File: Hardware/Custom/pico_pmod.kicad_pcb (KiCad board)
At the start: 2 copper layers, 50 x 37 mm, 22 parts, among them J1 Conn_02x06_Odd_Even, J2 Conn_02x06_Odd_Even, J3 Conn_02x06_Odd_Even, J4 USB_C_Receptacle_USB2.0, U1 RP2040

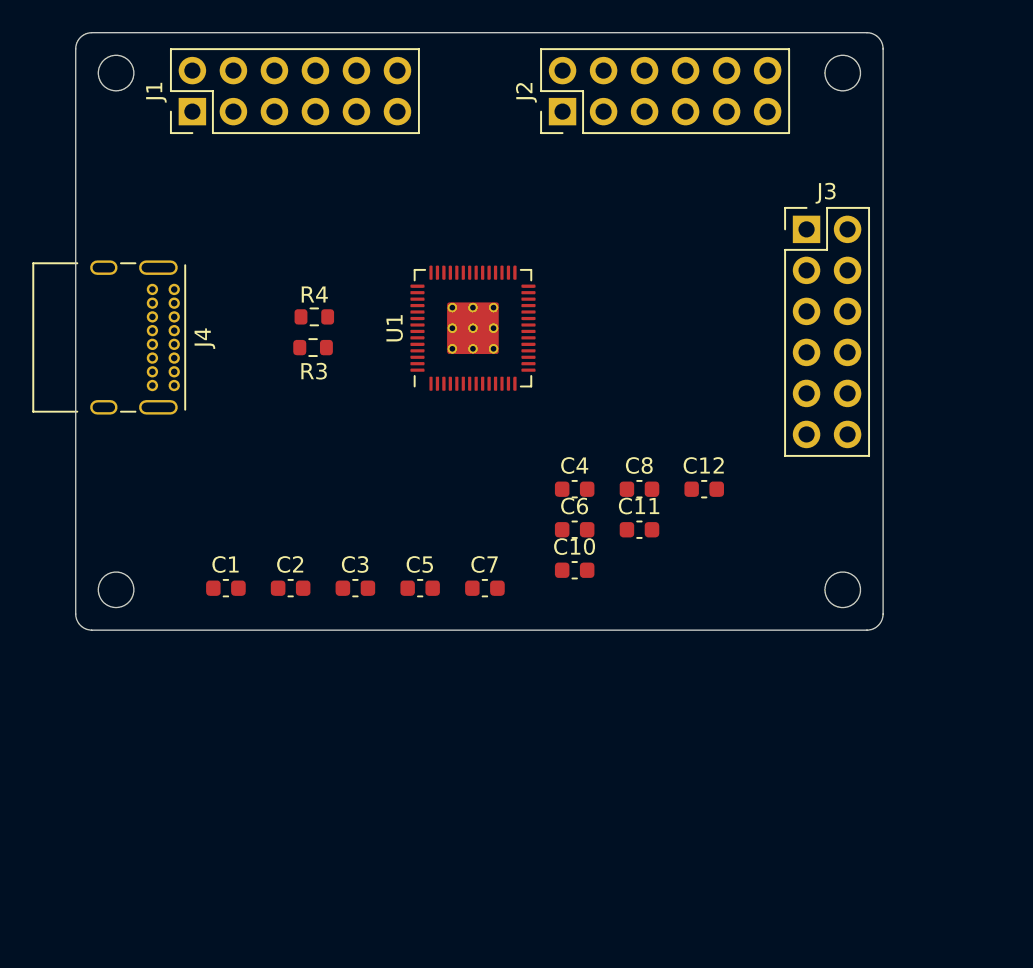
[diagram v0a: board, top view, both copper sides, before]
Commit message: Add the switchs footprints and put on PCB
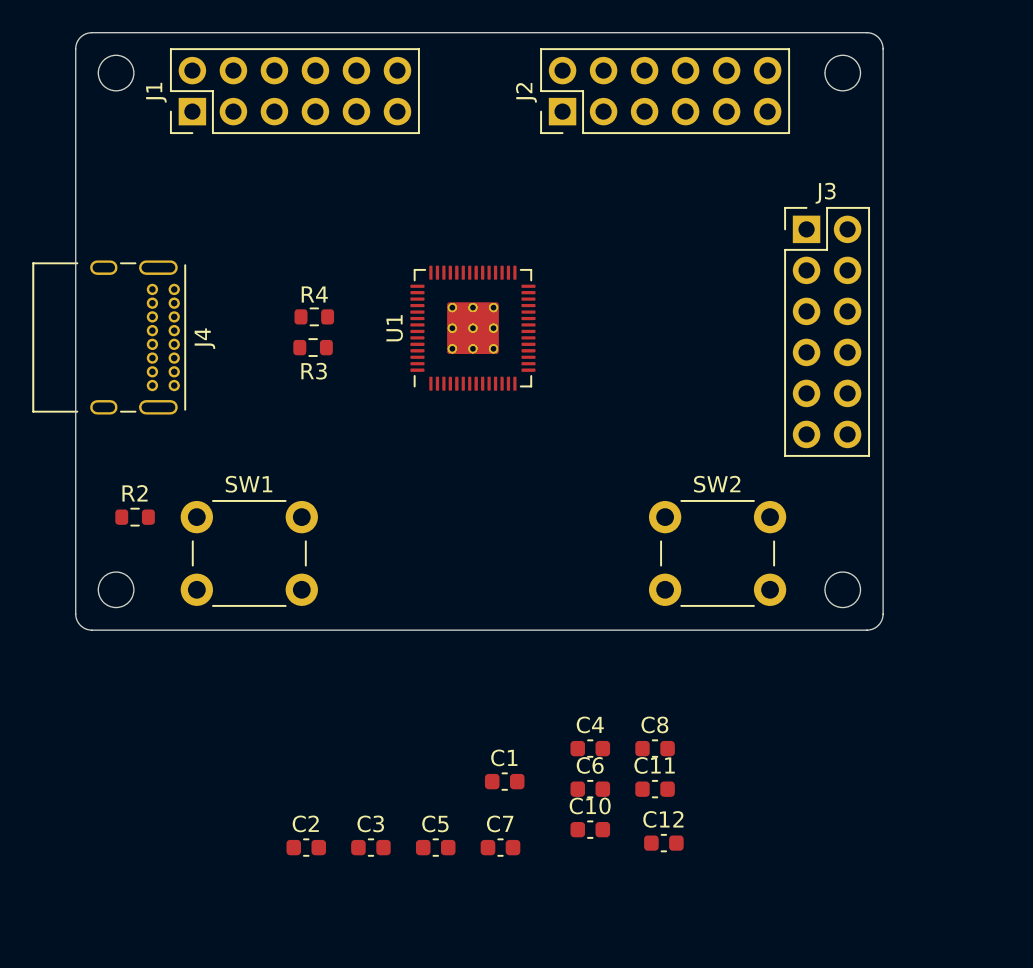
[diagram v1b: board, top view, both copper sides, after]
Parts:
- added R2: 1K, Resistor_SMD:R_0603_1608Metric, F.Cu at (126.7, 87.0)
- added SW1: SW_Push, Button_Switch_THT:SW_PUSH_6mm_H4.3mm, F.Cu at (130.5, 87.0)
- added SW2: SW_Push, Button_Switch_THT:SW_PUSH_6mm_H4.3mm, F.Cu at (159.5, 87.0)
- moved C12 22.1 mm to (159.4, 107.2)
- moved C1 21.0 mm to (149.6, 103.4)
- moved C10 16.1 mm to (154.9, 106.4)
- moved C11 16.1 mm to (158.9, 103.8)
- moved C2 16.1 mm to (137.3, 107.5)
- moved C3 16.1 mm to (141.3, 107.5)
- moved C4 16.1 mm to (154.9, 101.3)
- moved C5 16.1 mm to (145.3, 107.5)
- moved C6 16.1 mm to (154.9, 103.8)
- moved C7 16.1 mm to (149.3, 107.5)
- moved C8 16.1 mm to (158.9, 101.3)
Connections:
- J1 pad 1: GPIO_1 -> Net-(J1-Pad1)
- J1 pad 2: GPIO_0 -> Net-(J1-Pad2)
- J1 pad 3: GPIO_3 -> Net-(J1-Pad3)
- J1 pad 4: GPIO_2 -> Net-(J1-Pad4)
- J1 pad 5: GPIO_5 -> Net-(J1-Pad5)
- J1 pad 6: GPIO_4 -> Net-(J1-Pad6)
- J1 pad 7: GPIO_7 -> Net-(J1-Pad7)
- J1 pad 8: GPIO_6 -> Net-(J1-Pad8)
- J3 pad 1: Net-(J3-Pad1) -> GPIO_7
- J3 pad 2: Net-(J3-Pad2) -> GPIO_6
- J3 pad 3: Net-(J3-Pad3) -> GPIO_5
- J3 pad 4: Net-(J3-Pad4) -> GPIO_4
- J3 pad 5: Net-(J3-Pad5) -> GPIO_3
- J3 pad 6: Net-(J3-Pad6) -> GPIO_2
- J3 pad 7: Net-(J3-Pad7) -> GPIO_1
- J3 pad 8: Net-(J3-Pad8) -> GPIO_0

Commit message: Add usb CC 1 and 2 resistors
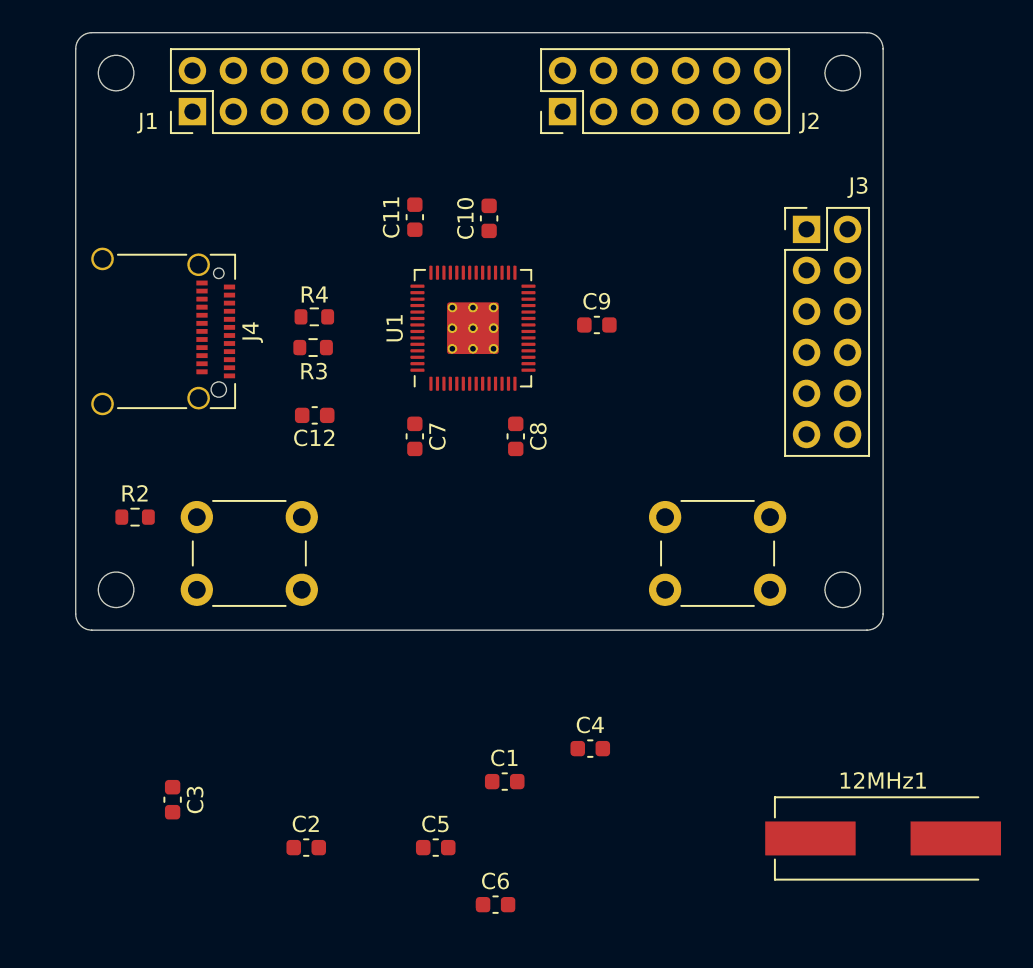
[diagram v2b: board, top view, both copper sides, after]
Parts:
- added 12MHz1: Crystal, RaspberryPi:Crystal_SMD_HC49-US, F.Cu at (173.0, 106.9)
- added C9: 100n, Capacitor_SMD:C_0603_1608Metric, F.Cu at (155.3, 75.1)
- C2, C4: value C -> 27p
- J4: footprint Connector_USB:USB_C_Receptacle_GCT_USB4085 -> Connector_USB:USB_C_Receptacle_Amphenol_12401610E4-2A_CircularHoles
- moved C11 38.4 mm to (144.0, 68.4), turned to 90 degrees
- moved C10 38.4 mm to (148.6, 68.5), turned to 90 degrees
- moved C12 34.2 mm to (137.8, 80.7), turned to 180 degrees
- moved C7 26.0 mm to (144.0, 82.0), turned to 270 degrees
- moved C8 21.2 mm to (150.2, 82.0), turned to 270 degrees
- moved C3 12.6 mm to (129.0, 104.5), turned to 270 degrees
- moved C6 9.25 mm to (149.0, 111.0)
- moved J4 3.05 mm to (127.5, 75.5)

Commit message: Add power supply and spi memory
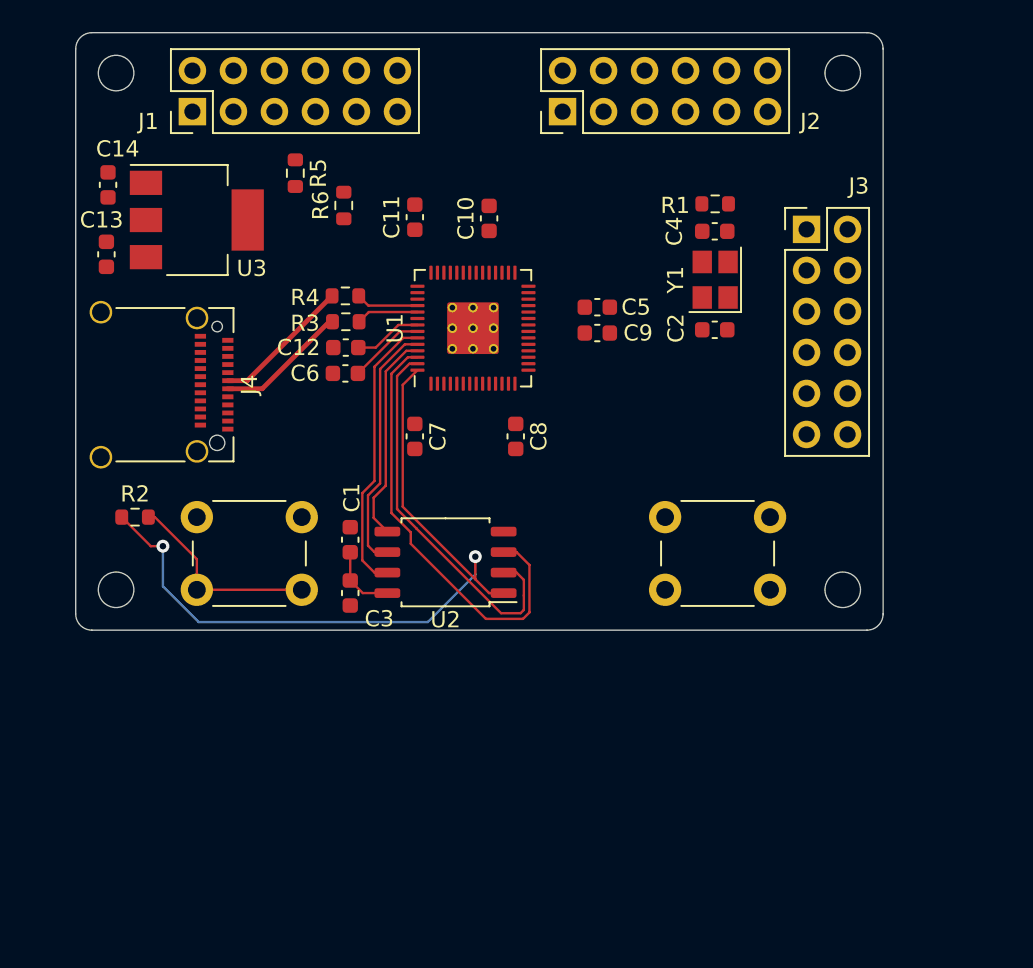
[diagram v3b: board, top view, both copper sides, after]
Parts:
- removed 12MHz1: Crystal, RaspberryPi:Crystal_SMD_HC49-US
- added C13: 10u, Capacitor_SMD:C_0603_1608Metric, F.Cu at (124.9, 70.7)
- added C14: 10u, Capacitor_SMD:C_0603_1608Metric, F.Cu at (125.0, 66.4)
- added R1: 1K, Resistor_SMD:R_0603_1608Metric, F.Cu at (162.6, 67.6)
- added R5: 5.1k, Resistor_SMD:R_0603_1608Metric, F.Cu at (136.6, 65.7)
- added R6: 5.1k, Resistor_SMD:R_0603_1608Metric, F.Cu at (139.6, 67.7)
- added U2: W25Q128JVS, Package_SO:SOIC-8_5.23x5.23mm_P1.27mm, F.Cu at (145.9, 89.8)
- added U3: NCP1117-3.3_SOT223, Package_TO_SOT_SMD:SOT-223-3_TabPin2, F.Cu at (130.5, 68.6)
- added Y1: 12MHz, Crystal:Crystal_SMD_SeikoEpson_FA238-4Pin_3.2x2.5mm, F.Cu at (162.6, 72.3)
- C2, C4: value 27p -> 20p
- moved C2 40.8 mm to (162.6, 75.4), turned to 180 degrees
- moved C5 34.9 mm to (155.3, 74.0)
- moved C6 34.2 mm to (139.7, 78.1), turned to 180 degrees
- moved C4 33.0 mm to (162.6, 69.3)
- moved C1 17.8 mm to (140.0, 88.4), turned to 90 degrees
- moved C3 16.9 mm to (140.0, 91.7)
- moved C12 4.62 mm to (139.7, 76.5)
- moved J4 3.30 mm to (127.4, 78.8)
- moved R3 2.58 mm to (139.7, 74.9)
- moved R4 2.32 mm to (139.7, 73.3)
- moved C9 0.50 mm to (155.3, 75.6)
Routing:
- net QSPI_SS: track 0.00 -> 47.9 mm, vias 0 -> 2
- net QSPI_SD2: track 0.00 -> 27.4 mm
- net QSPI_SD1: track 0.00 -> 23.7 mm
- net QSPI_SD3: track 0.00 -> 17.6 mm
- net QSPI_SCLK: track 0.00 -> 15.6 mm
- net QSPI_SD0: track 0.00 -> 13.1 mm
- net Net-(R2-Pad2): track 0.00 -> 12.5 mm
- net USB_DP: track 0.00 -> 8.63 mm
- net +3V3: track 0.00 -> 8.62 mm
- net USB_DN: track 0.00 -> 8.20 mm
- net +1V1: track 0.00 -> 4.76 mm
- net Net-(R4-Pad2): track 0.00 -> 3.89 mm
- net Net-(R3-Pad2): track 0.00 -> 3.86 mm
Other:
- rule trace_min: 0.2 -> 0.127

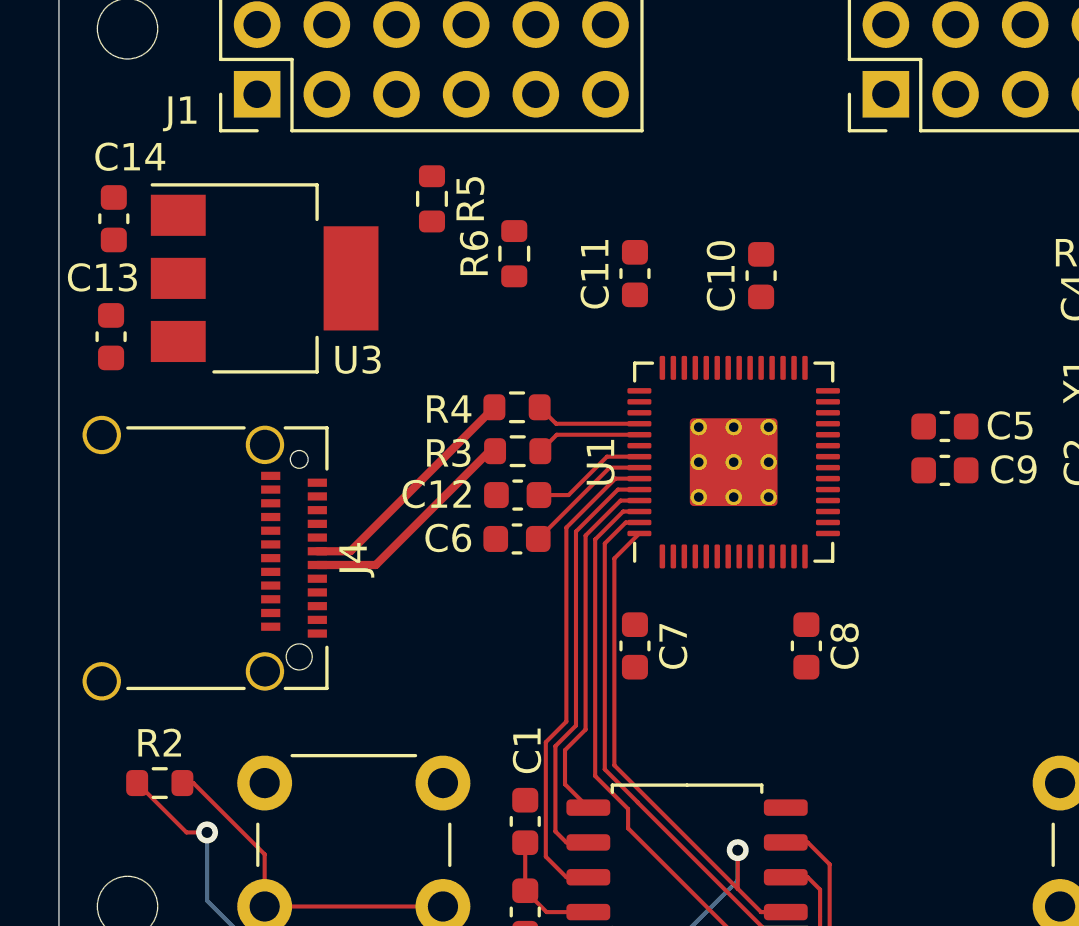
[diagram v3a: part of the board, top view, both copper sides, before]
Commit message: Add the USB resitors and route power supply
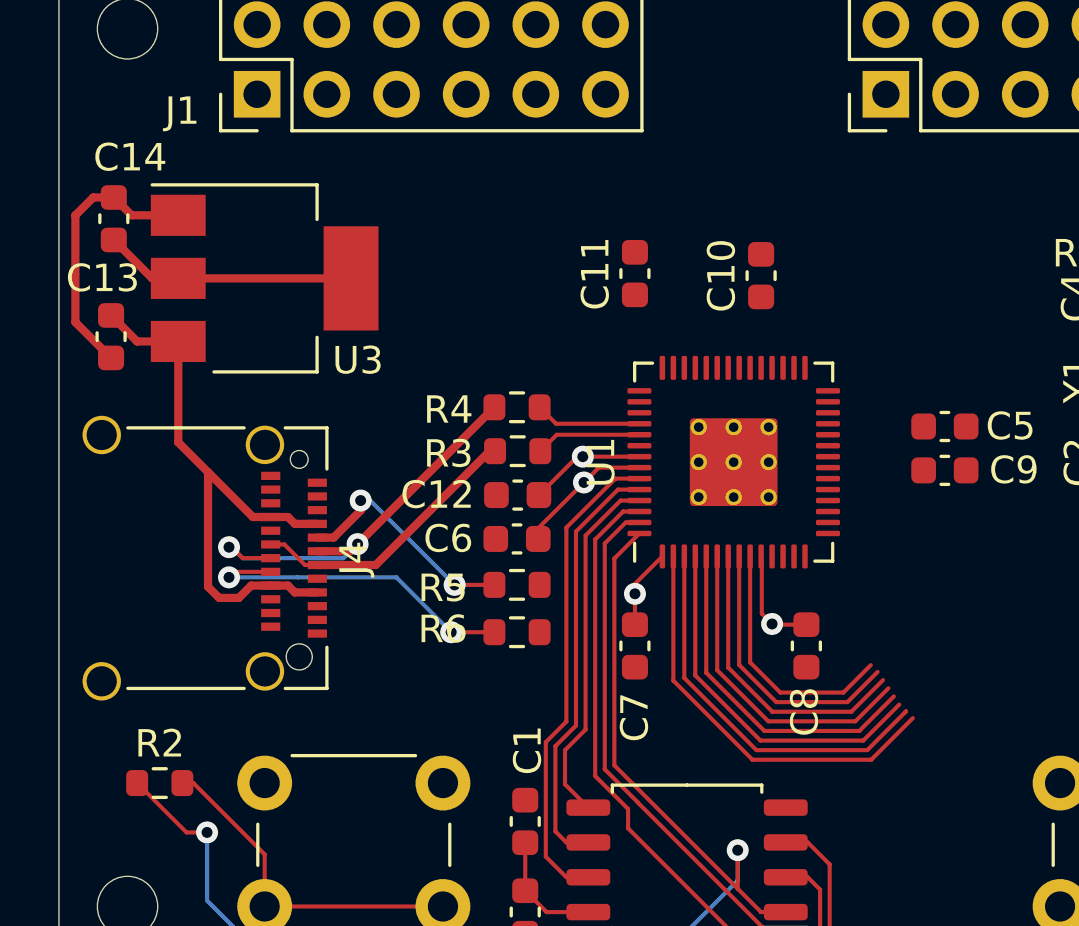
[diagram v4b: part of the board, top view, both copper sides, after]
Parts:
- moved R5 14.4 mm to (139.7, 79.8), turned to 180 degrees
- moved R6 13.8 mm to (139.7, 81.5), turned to 0 degrees
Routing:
- net VBUS: track 0.00 -> 21.4 mm
- net +3V3: track 8.62 -> 24.6 mm, vias 0 -> 3
- net GPIO_0: track 0.00 -> 15.1 mm
- net GPIO_1: track 0.00 -> 14.3 mm
- net GPIO_2: track 0.00 -> 13.3 mm
- net GPIO_3: track 0.00 -> 12.5 mm
- net Net-(J4-PadB5): track 0.00 -> 12.1 mm, vias 0 -> 2
- net GPIO_4: track 0.00 -> 11.7 mm
- net GPIO_5: track 0.00 -> 10.8 mm
- net GND: track 0.00 -> 10.0 mm
- net GPIO_6: track 0.00 -> 10.0 mm
- net GPIO_7: track 0.00 -> 9.13 mm
- net Net-(J4-PadA5): track 0.00 -> 8.60 mm, vias 0 -> 2
- net USB_DP: track 8.63 -> 15.4 mm, vias 0 -> 2
- net USB_DN: track 8.20 -> 10.2 mm
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
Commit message: Add the debug port footprint
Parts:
- added J5: Conn_01x04, Connector_PinHeader_2.54mm:PinHeader_1x04_P2.54mm_Vertical, F.Cu at (156.1, 103.9)
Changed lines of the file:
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@@
     (tracks 195)
     (zones 0)
-    (modules 34)
+    (modules 35)
     (nets 76)
   )
@@
     (add_net XOUT)
   )
+  (module Connector_PinHeader_2.54mm:PinHeader_1x04_P2.54mm_Vertical (layer F.Cu)
+    (at 156.1 103.9)
+    (descr "Through hole straight pin header, 1x04, 2.54mm pitch, single row")
+    (tags "Through hole pin header THT 1x04 2.54mm single row")
+    (fp_text reference J5 (at 0 -2.33) (layer F.SilkS)
+      (effects (font (size 1 1) (thickness 0.15)))
+    )
+    (fp_text value Conn_01x04 (at 0 9.95) (layer F.Fab)
+      (effects (font (size 1 1) (thickness 0.15)))
+    )
+    (fp_text user %R (at 0 3.81 90) (layer F.Fab)
+      (effects (font (size 1 1) (thickness 0.15)))
+    )
+    (fp_line (start -0.635 -1.27) (end 1.27 -1.27) (layer F.Fab) (width 0.1))
+    (fp_line (start 1.27 -1.27) (end 1.27 8.89) (layer F.Fab) (width 0.1))
+    (fp_line (start 1.27 8.89) (end -1.27 8.89) (layer F.Fab) (width 0.1))
+    (fp_line (start -1.27 8.89) (end -1.27 -0.635) (layer F.Fab) (width 0.1))
+    (fp_line (start -1.27 -0.635) (end -0.635 -1.27) (layer F.Fab) (width 0.1))
+    (fp_line (start -1.33 8.95) (end 1.33 8.95) (layer F.SilkS) (width 0.12))
+    (fp_line (start -1.33 1.27) (end -1.33 8.95) (layer F.SilkS) (width 0.12))
+    (fp_line (start 1.33 1.27) (end 1.33 8.95) (layer F.SilkS) (width 0.12))
+    (fp_line (start -1.33 1.27) (end 1.33 1.27) (layer F.SilkS) (width 0.12))
+    (fp_line (start -1.33 0) (end -1.33 -1.33) (layer F.SilkS) (width 0.12))
+    (fp_line (start -1.33 -1.33) (end 0 -1.33) (layer F.SilkS) (width 0.12))
+    (fp_line (start -1.8 -1.8) (end -1.8 9.4) (layer F.CrtYd) (width 0.05))
+    (fp_line (start -1.8 9.4) (end 1.8 9.4) (layer F.CrtYd) (width 0.05))
+    (fp_line (start 1.8 9.4) (end 1.8 -1.8) (layer F.CrtYd) (width 0.05))
+    (fp_line (start 1.8 -1.8) (end -1.8 -1.8) (layer F.CrtYd) (width 0.05))
+    (pad 4 thru_hole oval (at 0 7.62) (size 1.7 1.7) (drill 1) (layers *.Cu *.Mask)
+      (net 1 GND))
+    (pad 3 thru_hole oval (at 0 5.08) (size 1.7 1.7) (drill 1) (layers *.Cu *.Mask)
+      (net 38 SWDIO))
+    (pad 2 thru_hole oval (at 0 2.54) (size 1.7 1.7) (drill 1) (layers *.Cu *.Mask)
+      (net 37 SWCLK))
+    (pad 1 thru_hole rect (at 0 0) (size 1.7 1.7) (drill 1) (layers *.Cu *.Mask)
+      (net 2 +3V3))
+    (model ${KISYS3DMOD}/Connector_PinHeader_2.54mm.3dshapes/PinHeader_1x04_P2.54mm_Vertical.wrl
+      (at (xyz 0 0 0))
+      (scale (xyz 1 1 1))
+      (rotate (xyz 0 0 0))
+    )
+  )
   (module Package_TO_SOT_SMD:SOT-223-3_TabPin2 (layer F.Cu)
